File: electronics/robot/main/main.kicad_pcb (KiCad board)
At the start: 4 copper layers, 100 x 100 mm, 186 parts, among them M1 5mm, M2 5mm, M3 5mm, M4 16mm, M5 16mm, M6 16mm, P1 CONN_10, P14 CONN_8, P18 CONN_12, P2 CONN_30X2, P3 CONN_6, P4 CONN_4, P7 CONN_2, Q1 AO4882, Q10 AO4882, Q11 AO4882, Q12 AO4882, Q13 AO4882, Q14 MOSFET_N, Q15 MOSFET_N, Q16 AO4882, Q17 AO4882, Q2 AO4882, Q27 MOSFET_P, Q28 MOSFET_P, Q3 AO4882, Q4 AO4882, Q5 AO4882, Q6 AO4882, Q7 AO4882, Q8 AO4882, Q9 AO4882, SW1 SP3T, SW2 DIP6, U1 LM5107, U10 MCP1726, U11 7805, U12 ECS-3953M, U13 LM5107, U14 LM5107, U15 LM5107, U16 LM5107, U17 LM5107, U18 LM5107, U19 LM5107, U2 LM5107, U20 LM5107, U21 LM5107, U22 LM5107, U23 LP2951, U24 STM32F405RXT, U25 LIS3DH, U3 LM5107, U4 LM5107, U47 74HC4050, U5 LM5107, U6 BMG160, U7 MRF24J40MB, U8 XC6SLX9TQG144, U9 LD1117D33

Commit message: Fixed R4 reference.
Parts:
- R4: value 100K -> 100kR
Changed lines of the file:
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@@
-(kicad_pcb (version 4) (host pcbnew 4.0.1-stable)
+(kicad_pcb (version 4) (host pcbnew 4.0.2+dfsg1-2~bpo8+1-stable)
   (general
     (links 675)
@@
   )
   (layers
-    (0 Front signal)
-    (1 Ground power)
-    (2 VSupply power)
-    (31 Back signal)
-    (32 B.Adhes user)
-    (33 F.Adhes user)
-    (34 B.Paste user)
-    (35 F.Paste user)
+    (0 Front signal hide)
+    (1 Ground power hide)
+    (2 VSupply power hide)
+    (31 Back signal hide)
+    (32 B.Adhes user hide)
+    (33 F.Adhes user hide)
+    (34 B.Paste user hide)
+    (35 F.Paste user hide)
     (36 B.SilkS user)
     (37 F.SilkS user)
@@
       (effects (font (size 0.635 0.635) (thickness 0.127)))
     )
-    (fp_text value 100K (at 1.72974 -1.67894) (layer F.SilkS) hide
+    (fp_text value 100kR (at 1.72974 -1.67894) (layer F.SilkS) hide
       (effects (font (size 0.635 0.635) (thickness 0.127)))
     )

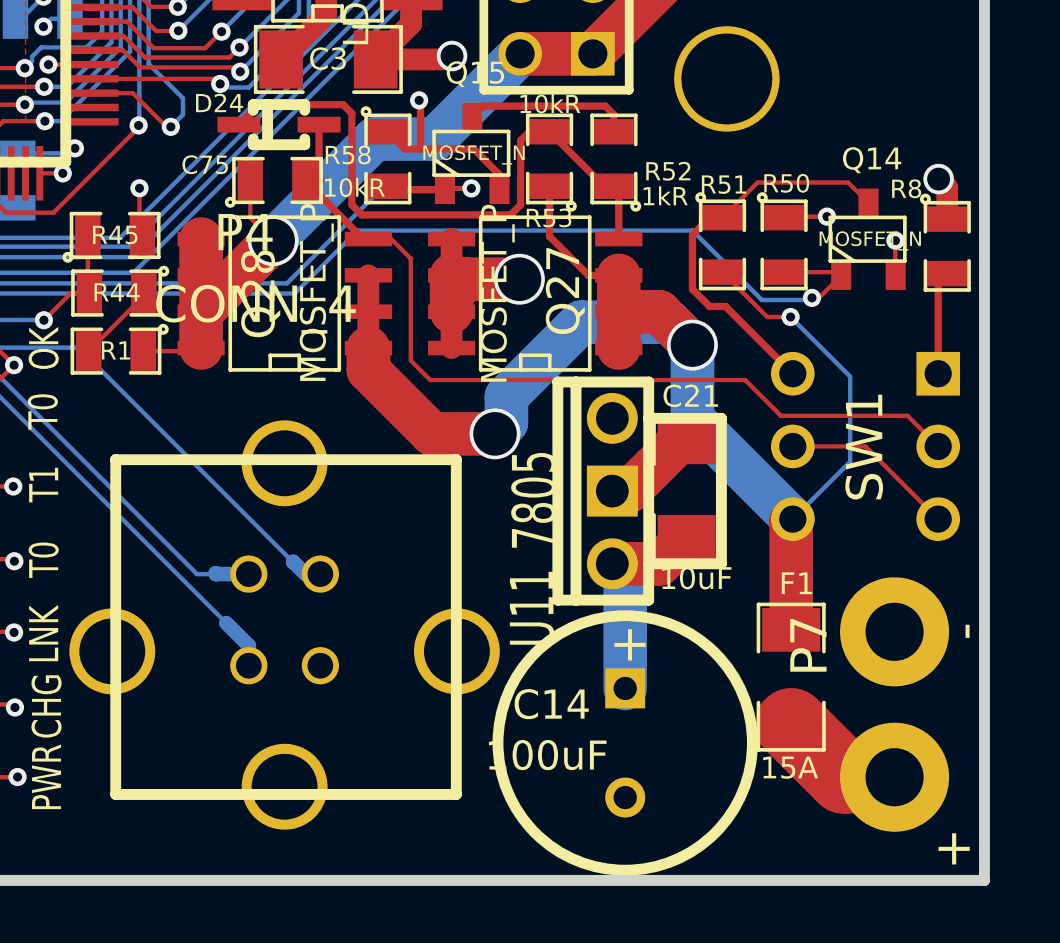
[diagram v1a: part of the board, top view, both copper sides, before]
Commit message: Fixed DNP capacitor and 15A_SLOW fuse issue on main board.
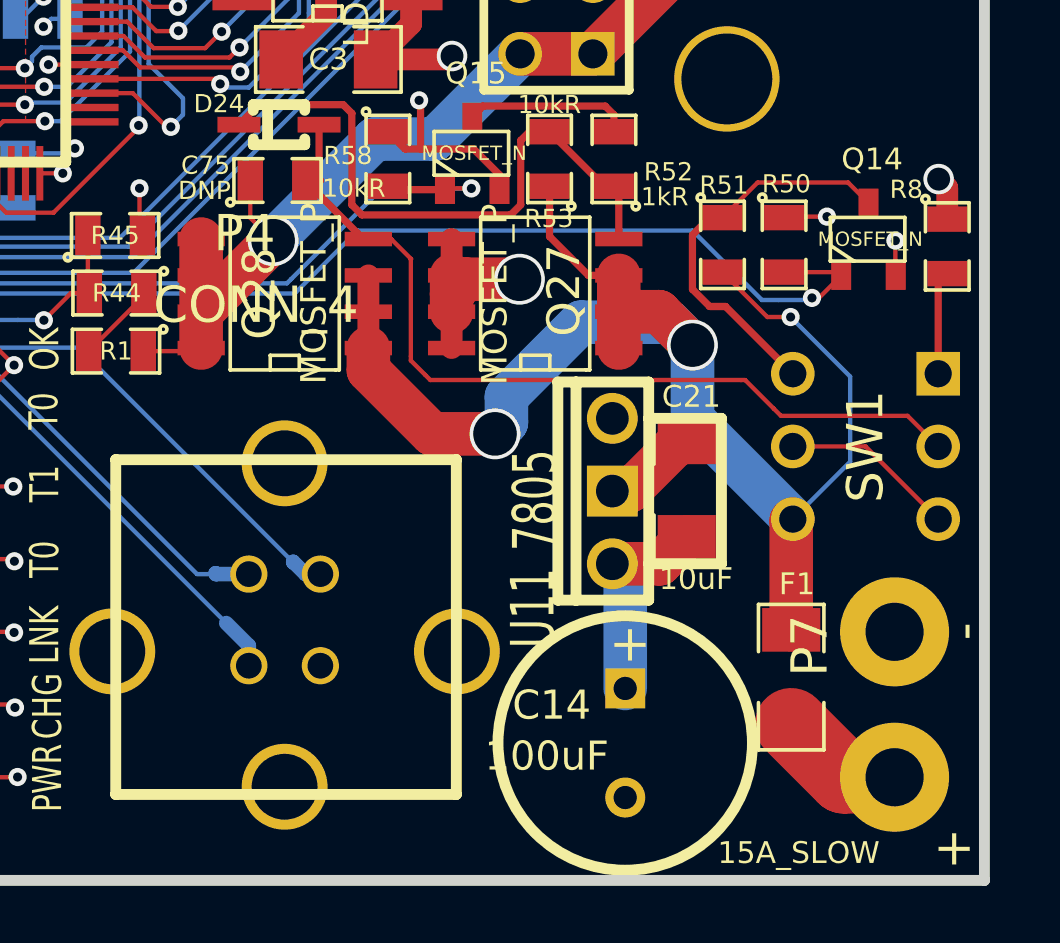
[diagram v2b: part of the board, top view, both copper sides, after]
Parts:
- C22: value 10uF -> 100nF
- F1: value 15A -> 15A_SLOW
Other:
- board text added: "DNP"
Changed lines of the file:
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@@
     (area 5.900056 13.61948 197.106578 183.248301)
     (thickness 1.6002)
-    (drawings 102)
+    (drawings 103)
     (tracks 4119)
     (zones 0)
@@
   )
   (layers
-    (0 Front signal hide)
+    (0 Front signal)
     (1 Ground power hide)
     (2 VSupply power hide)
     (31 Back signal hide)
     (32 B.Adhes user hide)
-    (33 F.Adhes user hide)
+    (33 F.Adhes user)
     (34 B.Paste user hide)
     (35 F.Paste user hide)
@@
       (effects (font (size 0.762 0.762) (thickness 0.127)))
     )
-    (fp_text value 15A (at -3.18516 -0.07112 180) (layer F.SilkS)
+    (fp_text value 15A_SLOW (at -6.14058 0.26088 360) (layer F.SilkS)
       (effects (font (size 0.762 0.762) (thickness 0.127)))
     )
@@
       (effects (font (size 0.635 0.635) (thickness 0.127)) (justify mirror))
     )
-    (fp_text value 10uF (at 2.72288 -0.43942 180) (layer B.SilkS) hide
+    (fp_text value 100nF (at 2.72288 -0.43942 180) (layer B.SilkS) hide
       (effects (font (size 0.635 0.635) (thickness 0.127)) (justify mirror))
     )
@@
       (net 194 GND))
   )
+  (gr_text DNP (at 133.75 107.9) (layer F.SilkS)
+    (effects (font (size 0.635 0.635) (thickness 0.15875)))
+  )
   (gr_line (start 105.37952 52.49926) (end 105.37952 52.451) (angle 90) (layer F.SilkS) (width 0.381))
   (gr_line (start 99.18954 52.49926) (end 105.37952 52.49926) (angle 90) (layer F.SilkS) (width 0.381))
@@
   (segment (start 158.4198 38.3286) (end 158.4198 46.4693) (width 0.1524) (layer Front) (net 191))
   (segment (start 157.861 128.397) (end 156.0957 128.397) (width 2.54) (layer Front) (net 192))
-  (segment (start 156.0957 128.397) (end 154.24912 126.55042) (width 2.54) (layer Front) (net 192))
+  (segment (start 156.0957 128.397) (end 154.24912 126.55042) (width 2.54) (layer Front) (net 192) (status 20))
   (segment (start 139.47648 114.17808) (end 141.69898 116.40058) (width 1.524) (layer Front) (net 193))
   (segment (start 153.416 112.3188) (end 151.84882 110.75162) (width 0.1524) (layer Front) (net 193))
@@
   (segment (start 139.47648 110.86338) (end 139.47648 112.13338) (width 0.762) (layer Front) (net 193))
   (segment (start 154.24912 119.43588) (end 154.305 119.38) (width 1.524) (layer Front) (net 193))
-  (segment (start 154.24912 123.24842) (end 154.24912 119.43588) (width 1.524) (layer Front) (net 193))
+  (segment (start 154.24912 123.24842) (end 154.24912 119.43588) (width 1.524) (layer Front) (net 193) (status 10))
   (via (at 150.7998 113.29924) (size 1.778) (drill 1.524) (layers Front Back) (net 193))
   (via (at 154.2288 112.3188) (size 0.635) (layers Front Back) (net 193))
